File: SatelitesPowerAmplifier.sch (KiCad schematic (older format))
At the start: 43 parts, among them P2 A/AB, P3 IN, P4 POWER, P5 OUT, Q1 КТ313В, Q10 КТ808А, Q11 КТ808А, Q2 КТ313В, Q3 КТ313В, Q4 КТ315, Q5 КТ313В, Q6 КТ313В, Q7 КТ940А, Q8 КТ961А, Q9 КТ961А

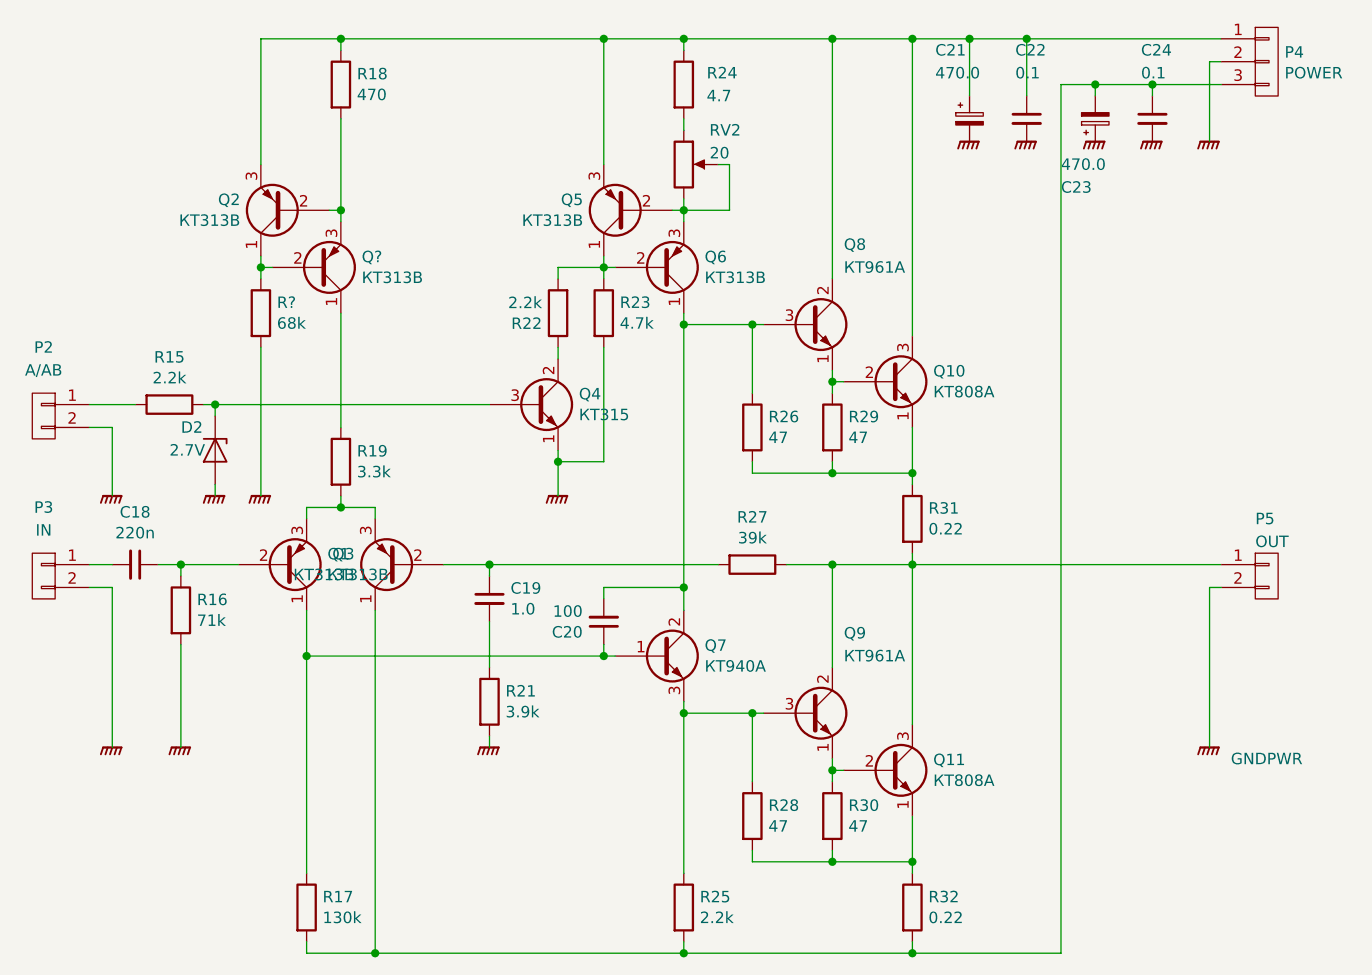
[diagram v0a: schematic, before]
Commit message: Add power to DAC
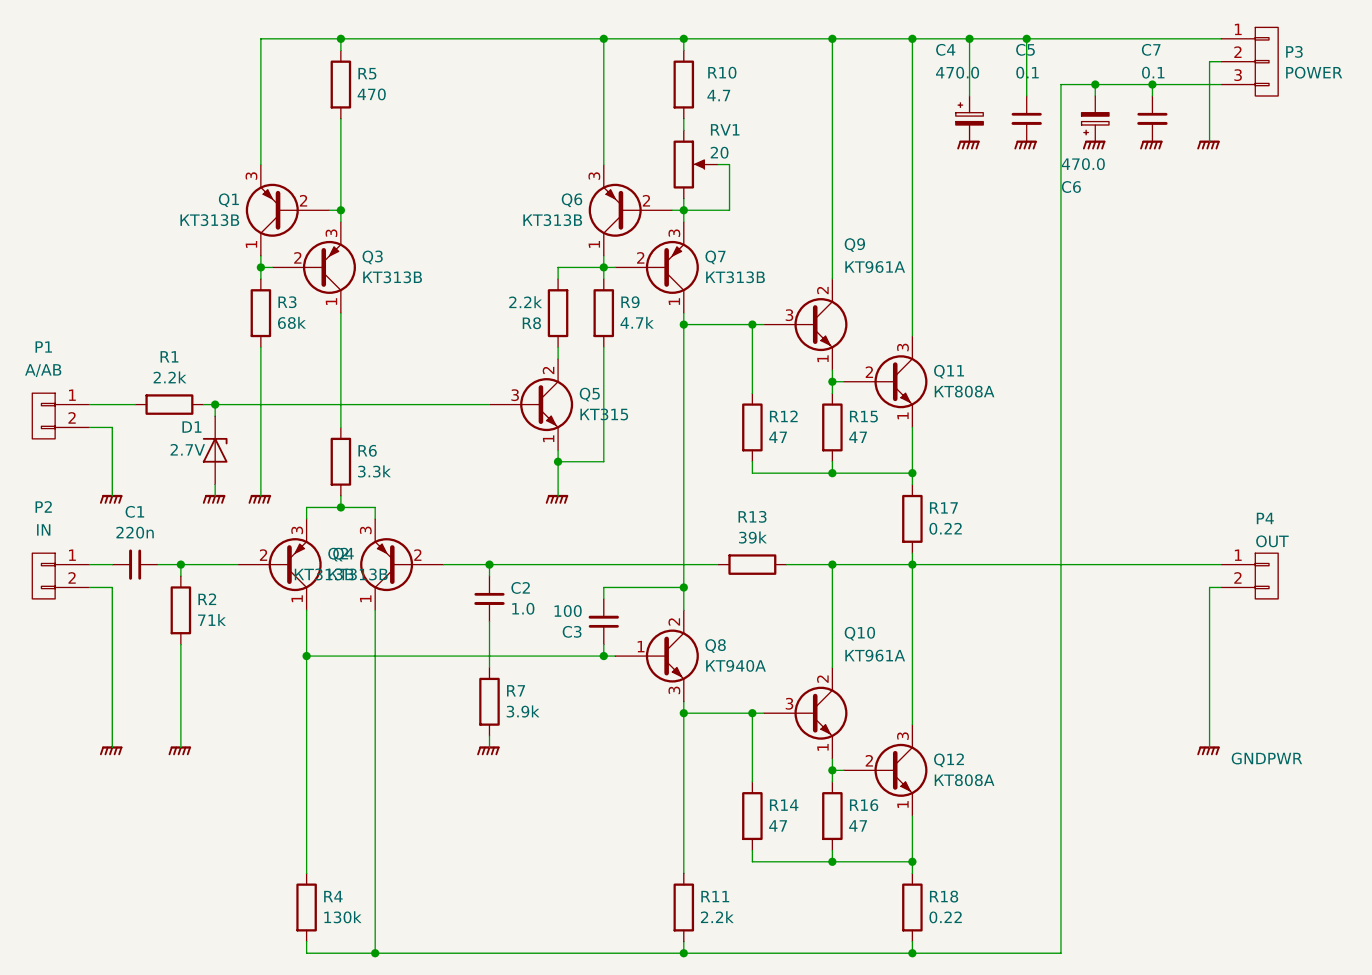
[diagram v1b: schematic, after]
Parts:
- gave numbers to parts that had none: 2
- renumbered C18 to C1, C19 to C2, C20 to C3, C21 to C4, C22 to C5, C23 to C6, C24 to C7, D2 to D1, P2 to P1, P3 to P2, P4 to P3, P5 to P4, Q2 to Q1, Q9 to Q10, Q10 to Q11, Q11 to Q12, Q1 to Q2, Q3 to Q4, Q4 to Q5, Q5 to Q6, Q6 to Q7, Q7 to Q8, Q8 to Q9, R15 to R1, R24 to R10, R25 to R11, R26 to R12, R27 to R13, R28 to R14, R29 to R15, R30 to R16, R31 to R17, R32 to R18, R16 to R2, R17 to R4, R18 to R5, R19 to R6, R21 to R7, R22 to R8, R23 to R9, RV2 to RV1

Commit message: Modify power amplifier
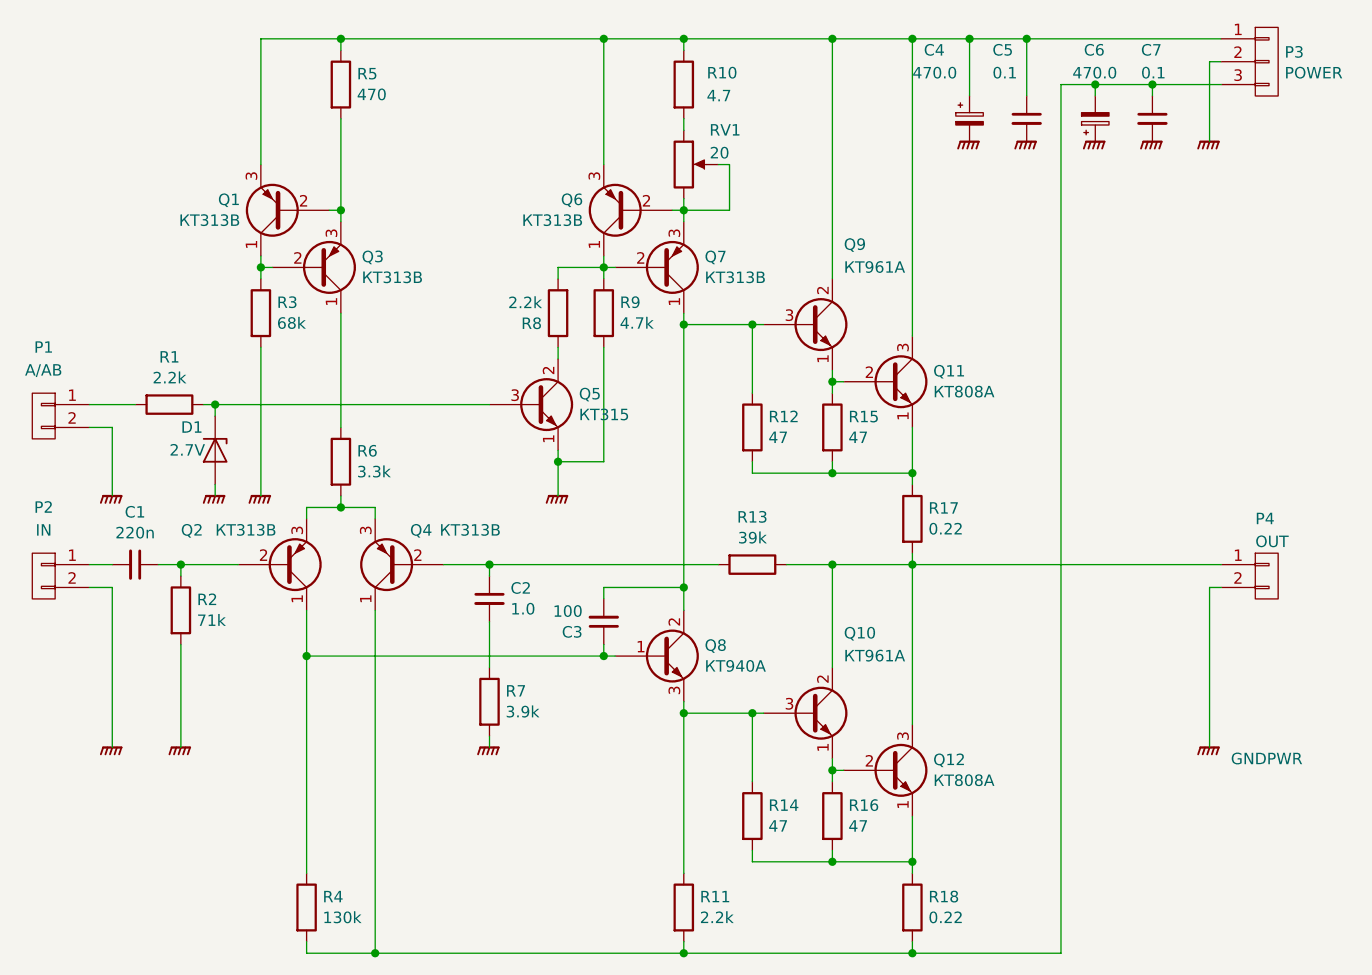
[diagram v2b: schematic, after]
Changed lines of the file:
@@
 EESchema Schematic File Version 4
 LIBS:amplifier-cache
-EELAYER 26 0
+EELAYER 30 0
 EELAYER END
 $Descr A4 11693 8268
@@
 U 1 1 588A2134
 P 6800 2100
-F 0 "C4" H 6650 2400 50  0000 L CNN
-F 1 "470.0" H 6650 2300 50  0000 L CNN
+F 0 "C4" H 6600 2400 50  0000 L CNN
+F 1 "470.0" H 6550 2300 50  0000 L CNN
 F 2 "" H 6800 2100 50  0001 C CNN
 F 3 "" H 6800 2100 50  0000 C CNN
@@
 U 1 1 588A227E
 P 7350 2100
-F 0 "C6" H 7200 2400 50  0000 L CNN
-F 1 "470.0" H 7200 2300 50  0000 L CNN
+F 0 "C6" H 7300 1800 50  0000 L CNN
+F 1 "470.0" H 7250 1900 50  0000 L CNN
 F 2 "" H 7350 2100 50  0001 C CNN
 F 3 "" H 7350 2100 50  0000 C CNN
@@
 U 1 1 588A22D0
 P 7050 2100
-F 0 "C5" H 7000 2400 50  0000 L CNN
-F 1 "0.1" H 7000 2300 50  0000 L CNN
+F 0 "C5" H 6900 2400 50  0000 L CNN
+F 1 "0.1" H 6900 2300 50  0000 L CNN
 F 2 "" H 7050 2100 50  0001 C CNN
 F 3 "" H 7050 2100 50  0000 C CNN
@@
 U 1 1 589880AA
 P 4300 4050
-F 0 "Q4" H 4490 4004 50  0000 L CNN
-F 1 "КТ313В" H 4490 4095 50  0000 L CNN
+F 0 "Q4" H 4150 3900 50  0000 L CNN
+F 1 "КТ313В" H 3850 3900 50  0000 L CNN
 F 2 "" H 4500 4150 50  0001 C CNN
 F 3 "" H 4300 4050 50  0000 C CNN
@@
 U 1 1 58988299
 P 3800 4050
-F 0 "Q2" H 3991 4004 50  0000 L CNN
-F 1 "КТ313В" H 3991 4095 50  0000 L CNN
+F 0 "Q2" H 3350 3900 50  0000 L CNN
+F 1 "КТ313В" H 3500 3900 50  0000 L CNN
 F 2 "" H 4000 4150 50  0001 C CNN
 F 3 "" H 3800 4050 50  0000 C CNN
